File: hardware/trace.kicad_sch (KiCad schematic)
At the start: 35 parts, among them J1 USB_C_Receptacle_USB2.0_16P, J2 Barrel_Jack_MountingPin, U1 LP2985-1.8, U10 IRS2092S, U11 INA240A1PW, U12 74AHCV17APW, U13 XPT2046TS, U14 INA253, U15 ATmega8U2-A, U16 AD7606, U17 THAT6261, U18 STM32F072RBIx, U19 FU540-C000, U2 LM317_SOT-223, U3 LM317L_SOT-89, U4 LTC6362xDD, U5 PAM8908, U6 CS4265, U7 MAX11120xTI, U8 SN65HVD255D, U9 74HC4024

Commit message: added stuff
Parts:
- removed C1: 0201, Capacitor_SMD:C_0201_0603Metric, symbol Device:C
- removed C2: 0402, Capacitor_SMD:C_0402_1005Metric, symbol Device:C
- removed C3: 0603, Capacitor_SMD:C_0603_1608Metric, symbol Device:C
- removed C4: 0805, Capacitor_SMD:C_0805_2012Metric, symbol Device:C
- removed C5: 1206, Capacitor_SMD:C_1206_3216Metric, symbol Device:C
- removed J1: USB_C_Receptacle_USB2.0_16P, Connector_USB:USB_C_Receptacle_GCT_USB4105-xx-A_16P_TopMnt_Horizontal, symbol Connector:USB_C_Receptacle_USB2.0_16P
- removed J2: Barrel_Jack_MountingPin, Connector_BarrelJack:BarrelJack_CUI_PJ-063AH_Horizontal, symbol Connector:Barrel_Jack_MountingPin
- removed U7: MAX11120xTI, Package_DFN_QFN:TQFN-28-1EP_5x5mm_P0.5mm_EP3.25x3.25mm, symbol Analog_ADC:MAX11120xTI
- added C10: 5, Capacitor_THT:CP_Radial_D5.0mm_P2.00mm, symbol Device:C_Polarized
- added C11: 10, Capacitor_SMD:CP_Elec_10x10.5, symbol Device:C_Polarized
- added C12: 8, Capacitor_SMD:CP_Elec_8x10.5, symbol Device:C_Polarized
- added C13: 6, Capacitor_SMD:CP_Elec_6.3x5.9, symbol Device:C_Polarized
- added C14: 5, Capacitor_SMD:CP_Elec_5x5.7, symbol Device:C_Polarized
- added C15: 4, Capacitor_SMD:CP_Elec_4x5.3, symbol Device:C_Polarized
- added C6: 10, Capacitor_THT:CP_Radial_D10.0mm_P5.00mm, symbol Device:C_Polarized
- added C7: 8, Capacitor_THT:CP_Radial_D8.0mm_P3.50mm, symbol Device:C_Polarized
- added C8: 6, Capacitor_THT:CP_Radial_D6.3mm_P2.50mm, symbol Device:C_Polarized
- added C9: 4, Capacitor_THT:CP_Radial_D4.0mm_P2.00mm, symbol Device:C_Polarized
- added D5: BAS16W, Package_TO_SOT_SMD:SOT-323_SC-70, symbol Diode:BAS16W
- added D6: 1.5SMCxxA, Diode_SMD:D_SMC, symbol Diode:1.5SMCxxA
- added D7: SMF5V0A, Diode_SMD:D_SMF, symbol Diode:SMF5V0A
- added L1: 1008, Inductor_SMD:L_1008_2520Metric, symbol Device:L
- added L2: 1210, Inductor_SMD:L_1210_3225Metric, symbol Device:L
- added L3: 1812, Inductor_SMD:L_1812_4532Metric, symbol Device:L
- added L4: 2512, Inductor_SMD:L_2512_6332Metric, symbol Device:L
- added L5: 6.3x6.3, Inductor_SMD:L_6.3x6.3_H3, symbol Device:L
- added L6: 7.3x7.3, Inductor_SMD:L_7.3x7.3_H4.5, symbol Device:L
- added L7: 10.4x10.4, Inductor_SMD:L_10.4x10.4_H4.8, symbol Device:L
- added Q1: DMG1012T, Package_TO_SOT_SMD:SOT-523, symbol Transistor_FET:DMG1012T
- added R6: 2010, Resistor_SMD:R_2010_5025Metric, symbol Device:R
- added R7: 2512, Resistor_SMD:R_2512_6332Metric, symbol Device:R
- added R8: 4020, Resistor_SMD:R_4020_10251Metric, symbol Device:R
- added R9: 1812, Resistor_SMD:R_1812_4532Metric, symbol Device:R
- added U20: INA181, Package_TO_SOT_SMD:SOT-23-6, symbol Amplifier_Current:INA181
- added U21: LTC6226xDC, Package_DFN_QFN:DFN-6-1EP_2x2mm_P0.5mm_EP0.6x1.37mm, symbol Amplifier_Operational:LTC6226xDC
- added U22: LTC2294xUP, Package_DFN_QFN:QFN-64-1EP_9x9mm_P0.5mm_EP7.15x7.15mm, symbol Analog_ADC:LTC2294xUP
- added U23: LTC6269xDD, Package_DFN_QFN:DFN-10-1EP_3x3mm_P0.5mm_EP1.65x2.38mm, symbol Amplifier_Operational:LTC6269xDD
- added U24: WM8731CLSEFL, Package_DFN_QFN:QFN-28-1EP_5x5mm_P0.5mm_EP3.35x3.35mm, symbol Audio:WM8731CLSEFL
- added U25: BQ25570, Package_DFN_QFN:QFN-20-1EP_3.5x3.5mm_P0.5mm_EP2x2mm, symbol Battery_Management:BQ25570
- added U26: IS31FL3733-TQ, Package_QFP:TQFP-48-1EP_7x7mm_P0.5mm_EP5x5mm, symbol Driver_LED:IS31FL3733-TQ
- added U27: PCA9685PW, Package_SO:TSSOP-28_4.4x9.7mm_P0.65mm, symbol Driver_LED:PCA9685PW
- added U28: SN74CB3Q3384APW, Package_SO:TSSOP-24_4.4x7.8mm_P0.65mm, symbol 74xx:SN74CB3Q3384APW
- added U29: AD630ARZ, Package_SO:SOIC-20W_7.5x12.8mm_P1.27mm, symbol Analog:AD630ARZ
- added U7: iC-HTG, Package_DFN_QFN:HVQFN-24-1EP_4x4mm_P0.5mm_EP2.5x2.5mm, symbol Driver_LED:iC-HTG
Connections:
- new net: U22.11 (REFLB), U22.12 (REFLB)
- new net: U22.13 (REFHB), U22.14 (REFHB)
- new net: U22.17 (GND), U22.64 (GND), U22.65 (GND)
- new net: U22.3 (REFHA), U22.4 (REFHA)
- new net: U22.31 (OGND), U22.50 (OGND)
- new net: U22.5 (REFLA), U22.6 (REFLA)
- new net: U26.12 (PGND), U26.5 (PGND)
- new net: U26.48 (GND), U26.49 (GND)
- new net: U21.3 (V-), U21.7 (V-)
- new net: U7.20 (GND), U7.25 (GND)
- new net: U24.19 (AGND), U24.29 (AGND)
- new net: U25.1 (VSS), U25.15 (VSS), U25.17 (VSS), U25.21 (VSS), U25.9 (VSS)
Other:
- note added: "BGA"
- note added: "DFN"
- moved on the sheet: U10, U11, U12A, U13, U14, U15, U16, U17A, U5, U8, U9

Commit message: stuff
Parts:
- removed U19: FU540-C000, Package_BGA:BGA-484_23.0x23.0mm_Layout22x22_P1.0mm, symbol MCU_SiFive:FU540-C000
- added C1: 0201, Capacitor_SMD:C_0201_0603Metric, symbol Device:C
- added C16: 1206, Capacitor_SMD:C_1206_3216Metric, symbol Device:C
- added C17: 1210, Capacitor_SMD:C_1210_3225Metric, symbol Device:C
- added C18: 1808, Capacitor_SMD:C_1808_4520Metric, symbol Device:C
- added C19: 1812, Capacitor_SMD:C_1812_4532Metric, symbol Device:C
- added C2: 0402, Capacitor_SMD:C_0402_1005Metric, symbol Device:C
- added C20: 1825, Capacitor_SMD:C_1825_4564Metric, symbol Device:C
- added C21: 2220, Capacitor_SMD:C_2220_5750Metric, symbol Device:C
- added C22: 2225, Capacitor_SMD:C_2225_5664Metric, symbol Device:C
- added C23: 3640, Capacitor_SMD:C_3640_9110Metric, symbol Device:C
- added C24: 3, Capacitor_SMD:CP_Elec_3x5.4, symbol Device:C_Polarized
- added C25: 7.5, Capacitor_THT:CP_Radial_D7.5mm_P2.50mm, symbol Device:C_Polarized
- added C3: 0504, Capacitor_SMD:C_0504_1310Metric, symbol Device:C
- added C4: 0603, Capacitor_SMD:C_0603_1608Metric, symbol Device:C
- added C5: 0805, Capacitor_SMD:C_0805_2012Metric, symbol Device:C
- added L10: 0603, Inductor_SMD:L_0603_1608Metric, symbol Device:L
- added L11: 0805, Inductor_SMD:L_0805_2012Metric, symbol Device:L
- added L12: 1206, Inductor_SMD:L_1206_3216Metric, symbol Device:L
- added L13: 1806, Inductor_SMD:L_1806_4516Metric, symbol Device:L
- added L14: 2010, Inductor_SMD:L_2010_5025Metric, symbol Device:L
- added L8: 0201, Inductor_SMD:L_0201_0603Metric, symbol Device:L
- added L9: 0402, Inductor_SMD:L_0402_1005Metric, symbol Device:L
- added R10: 0508, Resistor_SMD:R_0508_1220Metric, symbol Device:R
- added R11: 0612, Resistor_SMD:R_0612_1632Metric, symbol Device:R
- added R12: 0815, Resistor_SMD:R_0815_2038Metric, symbol Device:R
- added R13: 1020, Resistor_SMD:R_1020_2550Metric, symbol Device:R
- added R14: 1218, Resistor_SMD:R_1218_3246Metric, symbol Device:R
- added R15: 1225, Resistor_SMD:R_1225_3264Metric, symbol Device:R
- added R16: 2816, Resistor_SMD:R_2816_7142Metric, symbol Device:R
- C8: value 6 -> 6.3
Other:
- moved on the sheet: C10, C8, C9, U18

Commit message: README and board done
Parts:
- C1, C10, C11, C12, C13, C14, C15, C16, C17, C18, C19, C2, C20, C21, C22, C23, C24, C25, C3, C4, C5, C6, C7, C8, C9, D1, D2, D3, D4, D5, D6, D7, L1, L10, L11, L12, L13, L14, L2, L3, L4, L5, L6, L7, L8, L9, Q1, R1, R10, R11, R12, R13, R14, R15, R16, R2, R3, R4, R5, R6, R7, R8, R9, U1, U10, U11, U12, U13, U14, U15, U16, U17, U18, U2, U20, U21, U22, U23, U24, U25, U26, U27, U28, U29, U3, U4, U5, U6, U7, U8, U9: now not fitted
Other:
- note added: "General"
- note added: "PASSIVES"
- note added: "Trace"

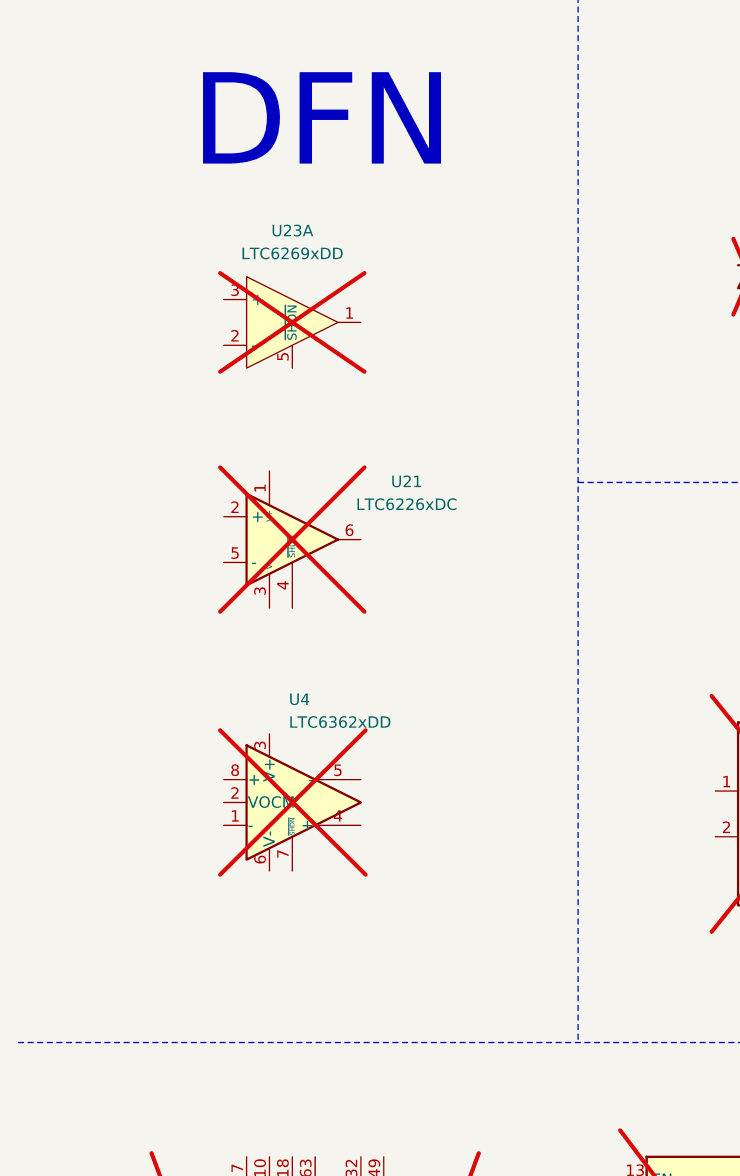
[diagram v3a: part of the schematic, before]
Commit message: add nfc
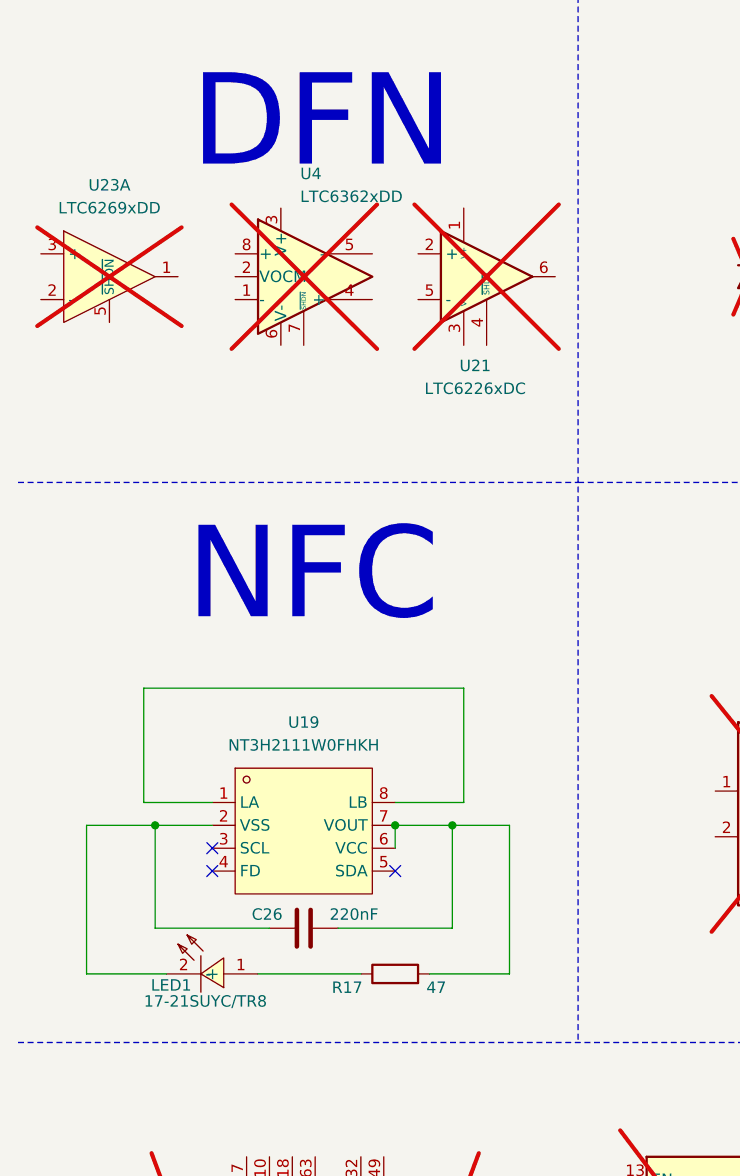
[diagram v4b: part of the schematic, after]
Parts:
- added C26: 220nF, Capacitor_SMD:C_0603_1608Metric, symbol Device:C
- added LED1: 17-21SUYC/TR8, lcsc:LED0805-R-RD, symbol lcsc:17-21SUYC_TR8
- added R17: 47, Resistor_SMD:R_0402_1005Metric, symbol Device:R
- added U19: NT3H2111W0FHKH, lcsc:XQFN-8_L1.6-W1.6-P0.50-BL_NT3H2111W0FHKH, symbol lcsc:NT3H2111W0FHKH
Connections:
- new net: U19.1 (LA), U19.8 (LB)
- new net: C26.1, LED1.2 (-), U19.2 (VSS)
- new net: C26.2, R17.2, U19.6 (VCC), U19.7 (VOUT)
- new net: LED1.1 (+), R17.1
- no-connect marks 0 -> 3
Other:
- note added: "NFC"
- moved on the sheet: U21, U23A, U4
